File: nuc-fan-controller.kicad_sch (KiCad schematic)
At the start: 38 parts, among them J1 19V IN, J2 NUC fan header, J3 FAN 1, J4 FAN 2, J5 Pro Mini, Q1 BC547B, Q2 BC547B, Q3 IRFZ44N, U1 LM2596T, U2 AMS1117-5.0, U3 AMS1117-3.3

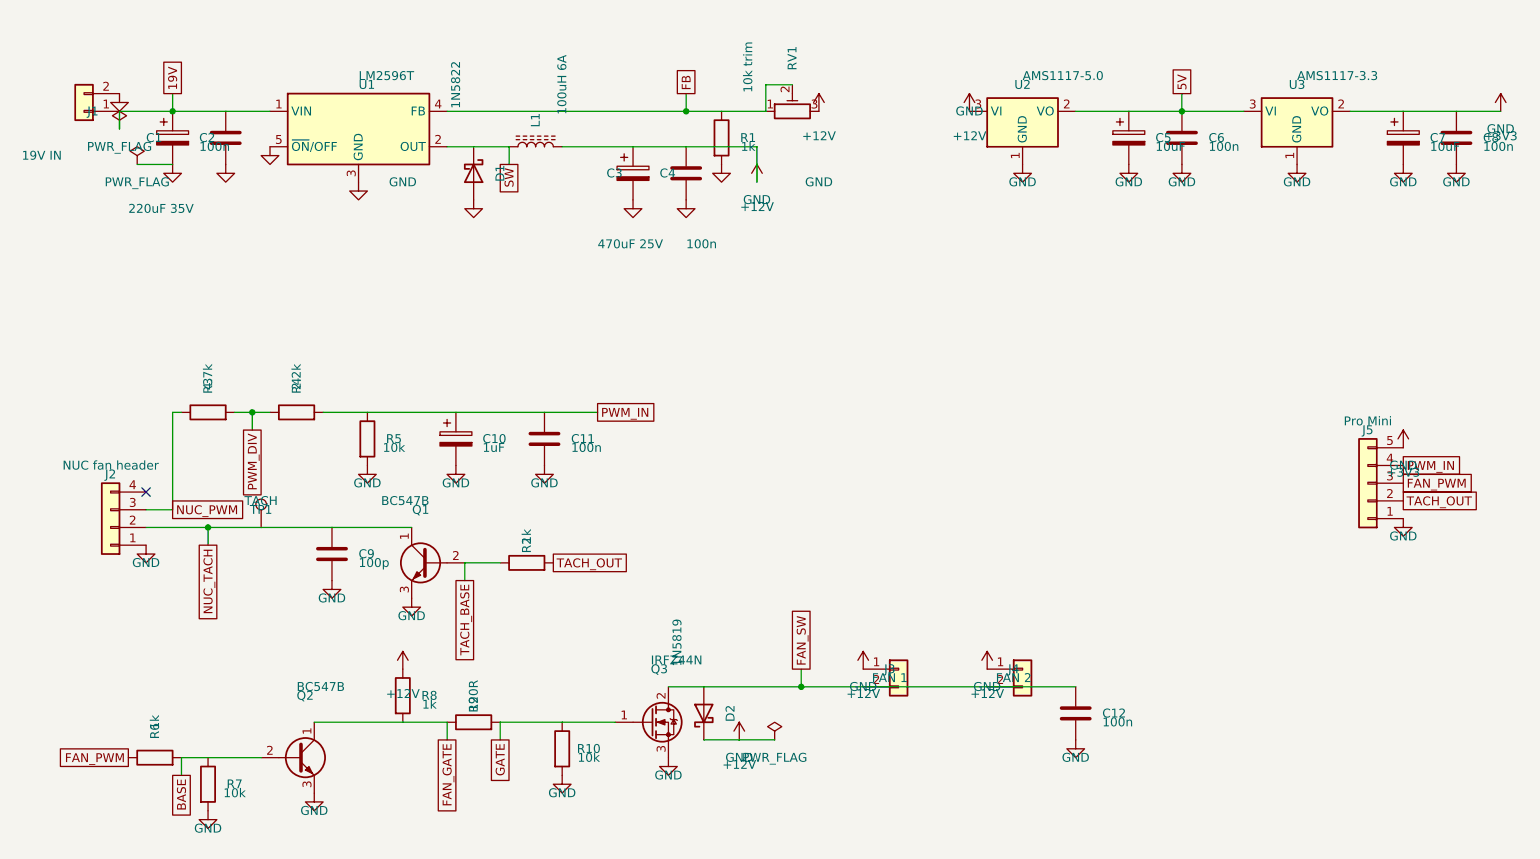
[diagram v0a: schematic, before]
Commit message: nuc-fan-controller: the 19V->12V converter is a module now, not parts on the board
Seven parts and their copper — U1 LM2596T-ADJ, L1 100 uH 6 A toroid, D1 1N5822,
C1 220u/35V, C2 100n, R1 1k, RV1 10k trim — are replaced by J6, a 1x04 header
(1,2 GND / 3 19V / 4 +12V) that a finished XL4016E1 step-down module from
cabinet L1 A10 plugs into. C3 470u/25V and C4 stay as the board's local
decoupling where the 12 V rail lands.

This reverses an earlier instruction: the XL4016E1 module had been ruled out and
the converter built from parts instead. The ruling is lifted. BUILD.md says so
out loud and carries the arithmetic that makes the module the better answer at
12 V / 1 A — 5-40 V in, 1.2-36 V out, 8 A, ~180 kHz, ~50 mV ripple; 0.16 A
inductor ripple at this load so it never enters discontinuous conduction and
never pulse-skips; 50 mV of rail ripple attenuated ~5000x by the PWM_IN
divider's time constant. The discrete design is in 10bc262 and every part of it
is still in the cabinet, so the swap goes both ways.

Schematic: 52 wires and 5 junctions, and they are exactly what logs/genwires.py
emits — logs/applywires.py is new and splices that set back into the .kicad_sch.
A pin or a name tag only connects to a wire END, so 19V is written as the segment
chain J1.1 -> (43.18,44.45) -> (48.26,44.45) -> J6.3, the vertices being where
the PWR_FLAG and the name tag hang off it; as one straight wire ERC reports both
as orphaned. ERC: 0 violations.

Board: J6 at (24,34); 19V routed J1 -> (18,34) -> (18,39.08) -> J6.3 and +12V
from J6.4 down and across onto the existing rail; the SW/FB/19V tracks, 22
dangling GND/+12V segments and one stray via deleted; zones refilled; the dead
SW netclass pattern removed; silkscreen beside J6 reads "1,2 GND 3 19V 4 12V".
DRC: 0 violations, 0 unconnected items, and the one documented parity warning —
J2 pin 4's deliberate no-connect.

exports/ rebuilt by logs/export.sh (new): BOM is 32 fitted parts, plus gerbers,
drill, placement, both board plots 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
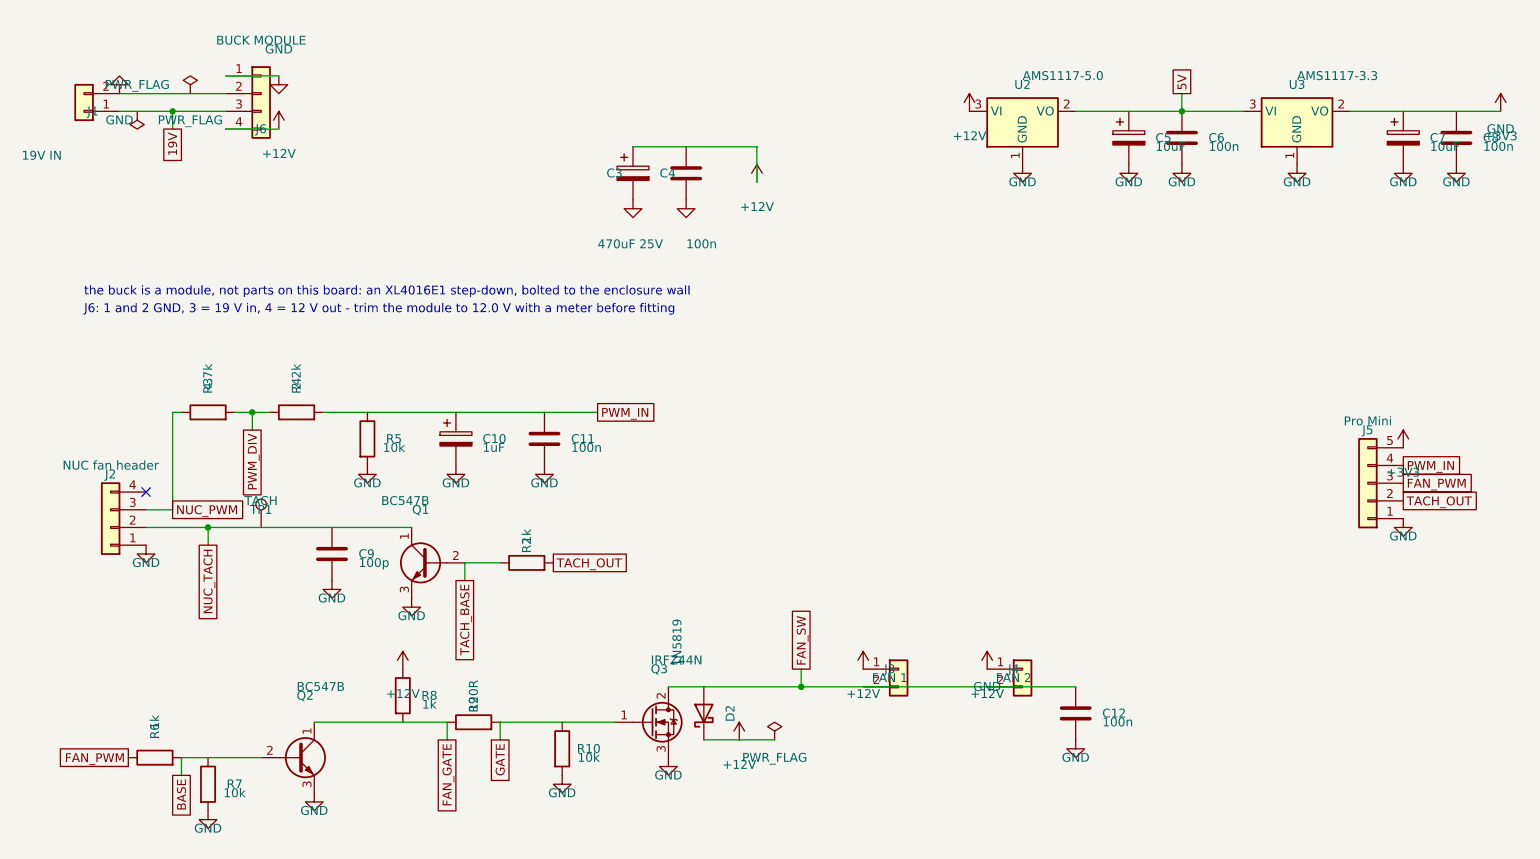
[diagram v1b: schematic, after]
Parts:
- removed C1: 220uF 35V, Capacitor_THT:CP_Radial_D10.0mm_P5.00mm, symbol Device:C_Polarized
- removed C2: 100n, Capacitor_THT:C_Disc_D3.8mm_W2.6mm_P2.50mm, symbol Device:C
- removed D1: 1N5822, Diode_THT:D_DO-201AD_P15.24mm_Horizontal, symbol Diode:1N5822
- removed L1: 100uH 6A, Inductor_THT:L_Toroid_Horizontal_D16.8mm_P14.70mm_Vishay_TJ3, symbol Device:L_Ferrite
- removed R1: 1k, Resistor_THT:R_Axial_DIN0204_L3.6mm_D1.6mm_P5.08mm_Horizontal, symbol Device:R
- removed RV1: 10k trim, Potentiometer_THT:Potentiometer_Bourns_3296W_Vertical, symbol Device:R_Potentiometer_Trim
- removed U1: LM2596T, Package_TO_SOT_THT:TO-220-5_P3.4x3.7mm_StaggerOdd_Lead3.8mm_Vertical, symbol Regulator_Switching:LM2596T-ADJ
- added J6: BUCK MODULE, Connector_PinHeader_2.54mm:PinHeader_1x04_P2.54mm_Vertical, symbol Connector_Generic:Conn_01x04
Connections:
- net +12V: now also J6.4 (Pin_4)
- net 19V: now also J6.3 (Pin_3)
- net GND: now also J6.1 (Pin_1), J6.2 (Pin_2)
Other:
- note added: "J6: 1 and 2 GND, 3 = 19 V in, 4 = 12 V out - trim the module to 12.0 V with a meter before fitting"
- note added: "the buck is a module, not parts on this board: an XL4016E1 step-down, bolted to the enclosure wall"

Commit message: schematic: name tags and power symbols moved onto the things they belong to
Hand pass in the KiCad editor. PWM_DIV now sits on the R3-R4 node itself instead
of on a stub; the +12V symbol sits on U2's VIN pin; the C3/C4 +12V stub is
shortened; J6's GND and +12V symbols move to either side of the header; TP1 is
flipped to hang on the tach line. 56 wires and 5 junctions.

ERC 0 violations. DRC with --schematic-parity: 0 violations, 0 unconnected items,
and the one documented J2 pin-4 no-connect warning — the board still matches.

Note for anyone regenerating: logs/genwires.py + applywires.py still describe the
pre-edit wire set (52 wires), so running them now would replace this routing and
orphan the symbols that moved. layout.py needs re-pointing at these positions
first.
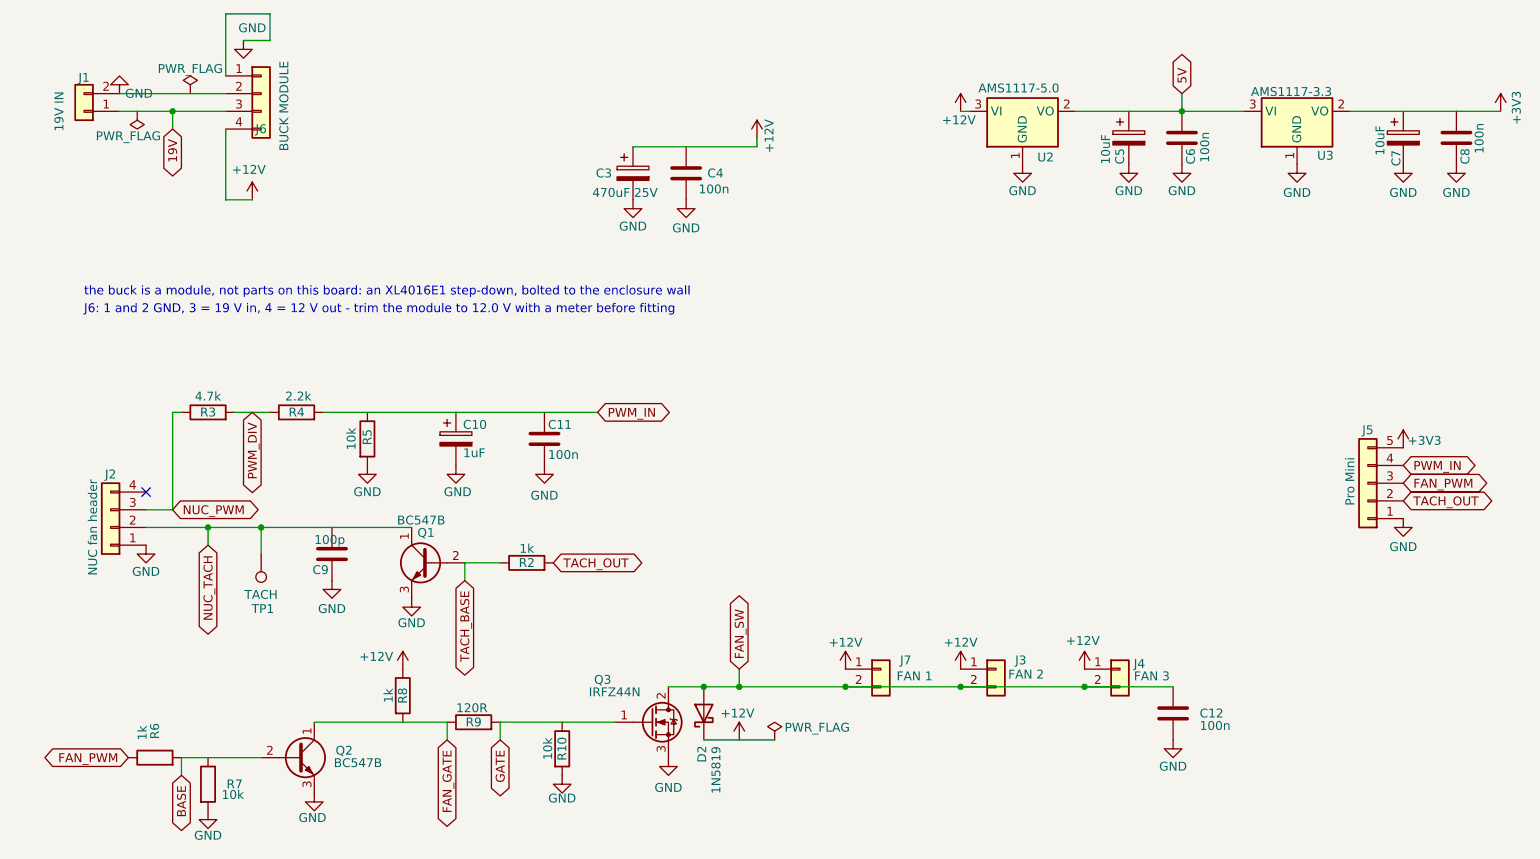
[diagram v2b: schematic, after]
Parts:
- added J7: FAN 1, Connector_PinHeader_2.54mm:PinHeader_1x02_P2.54mm_Vertical, symbol Connector_Generic:Conn_01x02
- J3: value FAN 1 -> FAN 2
- J4: value FAN 2 -> FAN 3
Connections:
- net +12V: now also J7.1 (Pin_1)
- net FAN_SW: now also J7.2 (Pin_2)
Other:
- moved on the sheet: C12, J3, J4, TP1

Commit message: Wire Q1/Q2 for the BC547s that are actually in the cabinet
The two transistors in R1 D3 are the NXP/Philips order — 1 emitter, 2 base,
3 collector. KiCad's Transistor_BJT:BC547 is the onsemi order (1 C, 2 B, 3 E), so
the schematic, the footprint pad numbers and the parts disagreed. Both symbols are
now Transistor_BJT:Q_NPN_EBC, which draws at identical pin coordinates and differs
only in the pin numbers: nothing on the drawing moved, the nets moved.

schematic (logs/fixq.py)
  Q1/Q2 -> Q_NPN_EBC, Sim.Pins 1=E 2=B 3=C, and the Datasheet link plus the
  Description now state the pinning. ERC 0 violations.

board (logs/fixboard.py, fixboard2.py, fixboard3.py)
  Pad 1 is the emitter on the GND pour, pad 3 the collector. NUC_TACH is re-run
  from Q1 pad 3 around the body onto the tach line at (109.73,18.782); FAN_GATE
  from Q2 pad 3 east to the existing run at (102.969,77.1109). The copper that used
  to hang off the old pads is gone: the GND feeds off Q1.3/Q2.3, the stubs into
  Q1.1/Q2.1, and the orphaned GND feed into R7.2 — R7 takes GND from the pour.
  BASE is jogged to y=74.75 so it clears Q2's now-live pad 1 by 0.40 mm instead of
  0.20, and two stitching vias in the new corridors plus a +12V via with copper on
  one layer only were removed. Silkscreen between the transistors reads
  "Q1 Q2 1=E 2=B 3=C"; pad 1 is the square pad.
  DRC 0 violations, 0 unconnected items, and the documented J2 pin-4 no-connect.

Update-from-schematic also brought in J7 (FAN 1 — the third fan connector) and
C12 100 n on FAN_SW, which were in the schematic but not on the board. J7 sits in
the fan column at (130,76) and is routed with the same bypass style the J3/J4 legs
use. That update had renamed FAN_SW to Net-(C12-Pad1) and PWM_DIV to Net-(R3-Pad2)
on the board, which drops both out of the Power net class, so the names were put
back by hand. BOM is 33 fitted parts.

Docs: BUILD.md gains "Which way round a BC547 goes" — meter them, a BC547B reads
hFE 200-450 forward and single digit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
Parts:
- Q1, Q2: symbol Transistor_BJT:BC547 -> Transistor_BJT:Q_NPN_EBC
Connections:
- net FAN_GATE: now also Q2.3 (C); no longer Q2.1 (C)
- net GND: now also Q1.1 (E), Q2.1 (E); no longer Q1.3 (E), Q2.3 (E)
- net NUC_TACH: now also Q1.3 (C); no longer Q1.1 (C)
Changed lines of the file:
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@@
 	)
 	(symbol
-		(lib_id "Transistor_BJT:BC547")
+		(lib_id "Transistor_BJT:Q_NPN_EBC")
 		(at 66.04 137.16 0)
 		(unit 1)
@@
 			)
 		)
-		(property "Datasheet" "https://www.onsemi.com/pub/Collateral/BC550-D.pdf"
+		(property "Datasheet" "https://doc.platan.ru/pdf/datasheets/philips/BC547.pdf"
 			(at 66.04 137.16 0)
 			(hide yes)
@@
 			)
 		)
-		(property "Description" "0.1A Ic, 45V Vce, Small Signal NPN Transistor, TO-92"
+		(property "Description" "0.1A Ic, 45V Vce, NPN small-signal transistor, TO-92 - 1=emitter 2=base 3=collector (NXP/Philips order)"
 			(at 66.04 137.16 0)
 			(hide yes)
@@
 	)
 	(symbol
-		(lib_id "Transistor_BJT:BC547")
+		(lib_id "Transistor_BJT:Q_NPN_EBC")
 		(at 85.09 109.22 0)
 		(mirror y)
@@
 			)
 		)
-		(property "Datasheet" "https://www.onsemi.com/pub/Collateral/BC550-D.pdf"
+		(property "Datasheet" "https://doc.platan.ru/pdf/datasheets/philips/BC547.pdf"
 			(at 85.09 109.22 0)
 			(hide yes)
@@
 			)
 		)
-		(property "Description" "0.1A Ic, 45V Vce, Small Signal NPN Transistor, TO-92"
+		(property "Description" "0.1A Ic, 45V Vce, NPN small-signal transistor, TO-92 - 1=emitter 2=base 3=collector (NXP/Philips order)"
 			(at 85.09 109.22 0)
 			(hide yes)

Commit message: Rebuild the board as one copper layer, 88.90 x 76.20 mm, for home etching
The board is now generated by logs/build1l.py instead of routed by Freerouting: parts,
drawn rails, holes, silkscreen and a small A* for the short legs all live in that script,
with footprint artwork cloned out of the KiCad 10 libraries by logs/getfp.py into
logs/fp-templates.inc.  logs/setrules.py writes the home-etch rules into the project.

Rules: clearance and minimum track 0.70 mm, drawn rails 1.80 mm, copper-to-edge 0.50 mm,
minimum drill 0.90 mm, maximum pad 1.80 mm, pour minimum thickness 0.80 mm.  Every layer
is F.Cu, and F.Cu is the component side, so the copper that gets etched is the copper the
parts solder to and nothing about the board is mirrored.

The ground pour is one island of 5009 mm2 with `connect_pads yes` -- the token matters:
KiCad 10 reads a bare `(connect_pads (clearance 0.7))` as thermal relief and stops the fill
0.70 mm short of every GND pad, which passes DRC and leaves the pads sitting in resin.
Traces of a foreign net keep the pour off, tracks of the pour's own net are absorbed by it,
which is why the router keeps a 2.20 mm gap (2 x clearance + min_thickness) between thin
copper so the fill never gets walled into pockets.

Nets that would fight each other are drawn as bars rather than handed to the router --
+12V, FAN_SW, 19V, +3V3, FAN_PWM, NUC_TACH, NUC_PWM, TACH_OUT, TACH_BASE, PWM_IN -- because
a long leg left to the A* escapes to the board perimeter and walls the pour off.  One
crossing cannot be routed around on a single layer: the Pro Mini's A0 and D11 sit side by
side and their destinations are on opposite sides of the divider row, so R11, a 0 Ohm
bridge, carries FAN_PWM over that row.  R11 is a board part only; the schematic has no such
component, and KiCad's board-only ratsnest therefore reports the join as a missing
connection, which is why that rule is downgraded to a warning and logs/verify.py checks the
real thing instead.

logs/verify.py and logs/p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
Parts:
- removed C5: 10uF, Capacitor_THT:CP_Radial_D6.3mm_P2.50mm, symbol Device:C_Polarized
- removed C6: 100n, Capacitor_THT:C_Disc_D3.8mm_W2.6mm_P2.50mm, symbol Device:C
- removed U2: AMS1117-5.0, Package_TO_SOT_SMD:SOT-223-3_TabPin2, symbol Regulator_Linear:AMS1117-5.0
- C10: footprint Capacitor_THT:CP_Radial_D8.0mm_P3.50mm -> Capacitor_THT:CP_Radial_D6.3mm_P2.50mm
- C12, C4: footprint Capacitor_THT:C_Disc_D3.8mm_W2.6mm_P2.50mm -> Capacitor_THT:C_Disc_D6.0mm_W2.5mm_P5.00mm
- C3: footprint Capacitor_THT:CP_Radial_D10.0mm_P5.00mm -> Capacitor_THT:CP_Radial_D8.0mm_P3.50mm
- C9: footprint Capacitor_THT:C_Disc_D3.0mm_W2.0mm_P2.50mm -> Capacitor_THT:C_Disc_D3.8mm_W2.6mm_P2.50mm
- U3: footprint Package_TO_SOT_SMD:SOT-223-3_TabPin2 -> Package_TO_SOT_SMD:TO-252-3_TabPin2
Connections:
- net 5V is gone; now on net +12V: U3.3 (VI)
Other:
- note added: "U3 takes 12 V straight off the module: this board has no 5 V rail, and a drive's 5 V must never come from here"
